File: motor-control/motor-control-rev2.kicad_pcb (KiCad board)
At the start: 2 copper layers, 122.3 x 65.9 mm, 80 parts, among them P1 CONN_02X12, P2 to_motor_phase_1, P3 to_motor_phase_2, P4 to_motor_phase_3, P5 CONN_01X01, P6 CONN_01X01, P7 CONN_01X04, Q1 csd19505kcs, Q10 csd19505kcs, Q11 csd19505kcs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

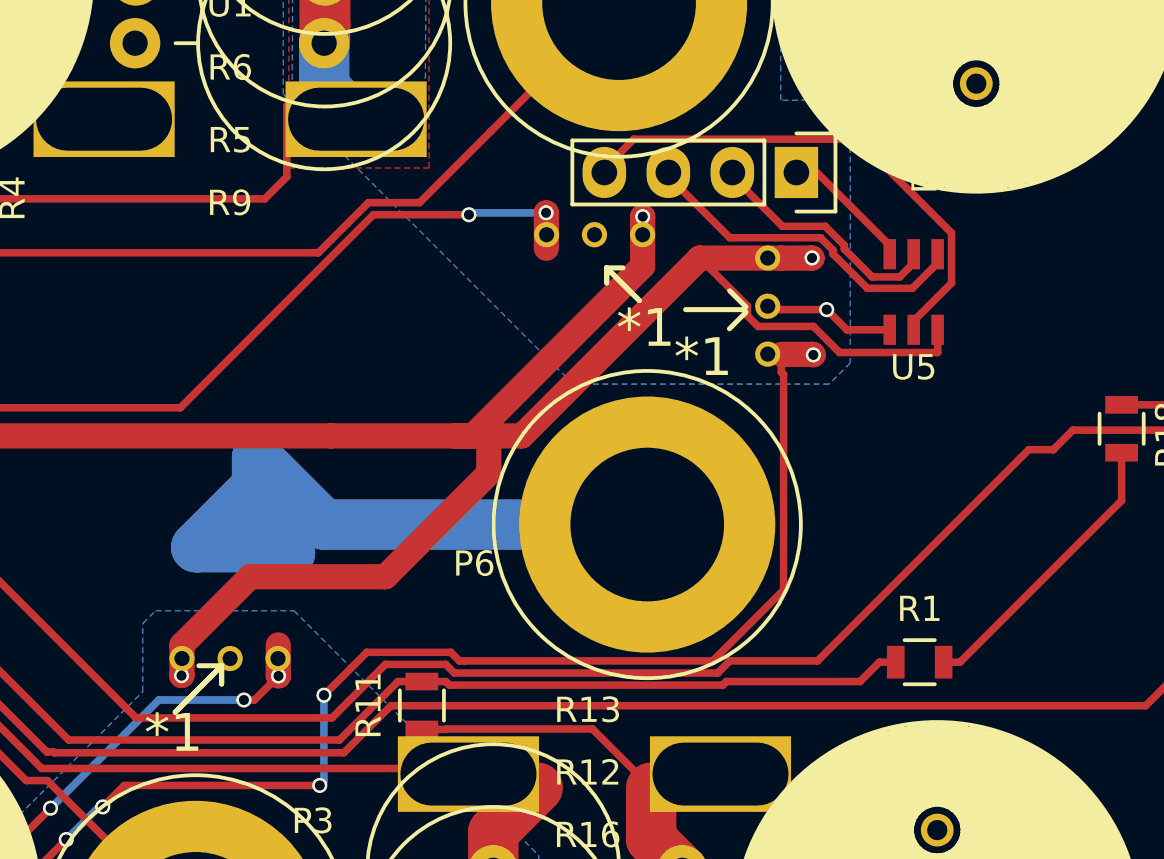
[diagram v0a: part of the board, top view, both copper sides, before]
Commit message: Added hall filtering components to pcb
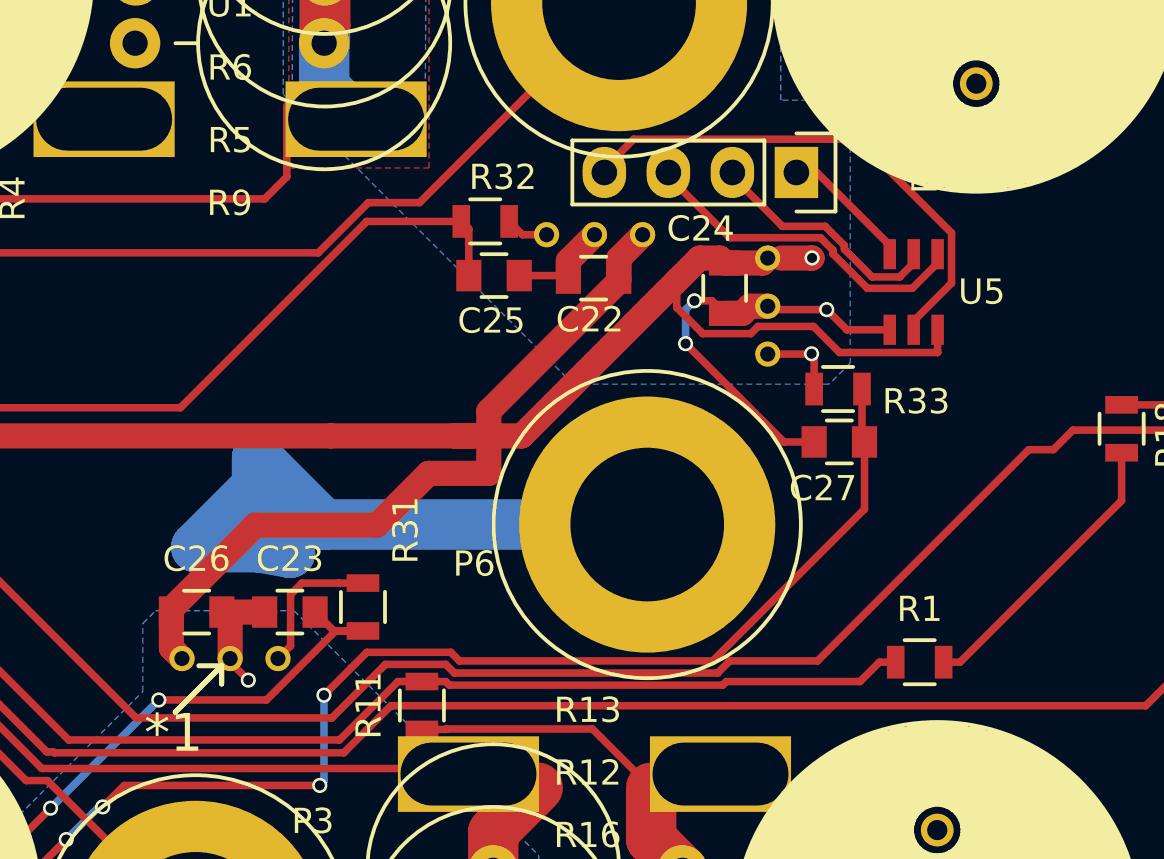
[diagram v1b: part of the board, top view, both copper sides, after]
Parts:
- added C22: 0.1uF, Capacitors_SMD:C_0805, F.Cu at (165.8, 80.2)
- added C23: 0.047uF, Capacitors_SMD:C_0805, F.Cu at (153.8, 93.4)
- added C24: 0.1uF, Capacitors_SMD:C_0805, F.Cu at (171.1, 80.5)
- added C25: 0.047uF, Capacitors_SMD:C_0805, F.Cu at (161.9, 80.0)
- added C26: 0.1uF, Capacitors_SMD:C_0805, F.Cu at (150.1, 93.4)
- added C27: 0.047uF, Capacitors_SMD:C_0805, F.Cu at (175.6, 86.7)
- added R31: 100R, Resistors_SMD:R_0805, F.Cu at (156.7, 93.2)
- added R32: 100R, Resistors_SMD:R_0805, F.Cu at (161.6, 77.9)
- added R33: 100R, Resistors_SMD:R_0805, F.Cu at (175.6, 84.5)
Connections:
- U1 pad 3: /power mosfets & current sensing/hall_1 -> Net-(R31-Pad1)
- U2 pad 3: /power mosfets & current sensing/hall_2 -> Net-(R32-Pad1)
- U3 pad 3: /power mosfets & current sensing/hall_3 -> Net-(R33-Pad2)
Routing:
- net GND: track 98.5 -> 119.2 mm, vias 9 -> 12
- net Net-(R31-Pad1): track 0.00 -> 5.81 mm
- net /power mosfets & current sensing/hall_1: track 51.4 -> 56.4 mm, vias 5 -> 4
- net Net-(R33-Pad2): track 0.00 -> 3.19 mm, vias 0 -> 1
- net /power mosfets & current sensing/hall_2: track 72.6 -> 70.0 mm, vias 4 -> 2
- net Net-(R32-Pad1): track 0.00 -> 1.70 mm
- net /power mosfets & current sensing/hall_3: track 76.6 -> 75.3 mm, vias 5 -> 4
- net VCC: track 183.9 -> 184.5 mm, vias 7 -> 5

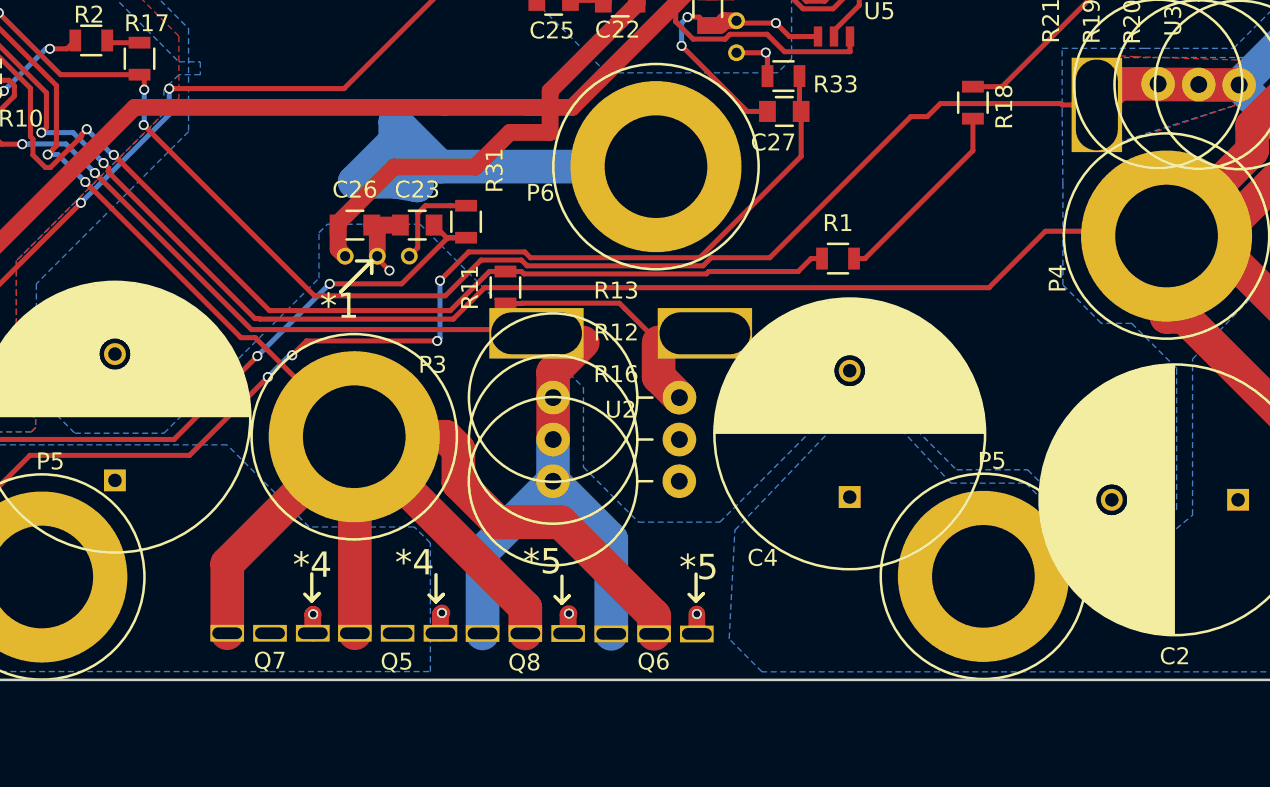
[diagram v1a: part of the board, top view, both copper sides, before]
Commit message: Began rework bottom fets spacing
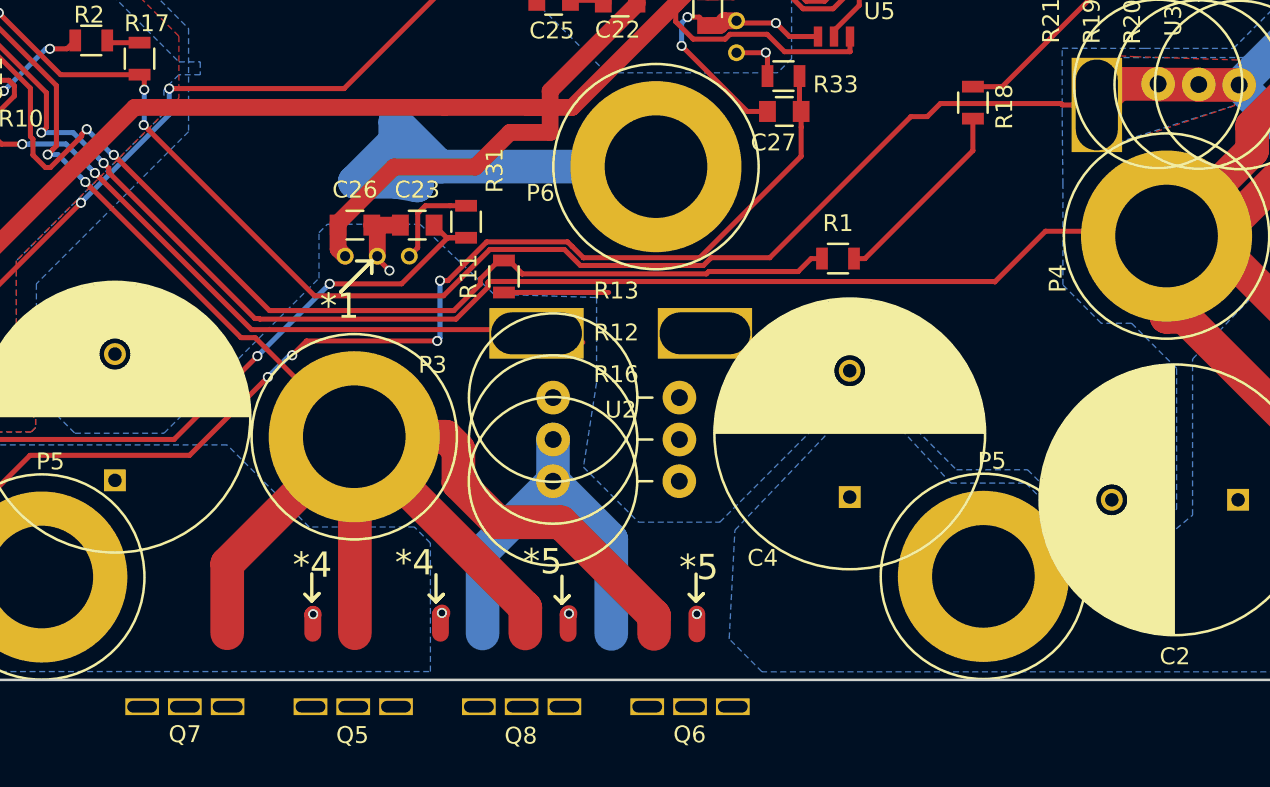
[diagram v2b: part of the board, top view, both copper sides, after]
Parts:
- moved Q7 6.68 mm to (140.0, 122.0)
- moved Q5 5.10 mm to (150.0, 122.0)
- moved Q6 4.82 mm to (170.0, 122.0)
- moved Q8 4.35 mm to (160.0, 122.0)
- moved R11 0.66 mm to (158.9, 96.5)
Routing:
- net GND: track 119.2 -> 111.6 mm
- net /Gate-Driver/SL_B: track 90.0 -> 83.5 mm
- net /Gate-Driver/SP2: track 68.8 -> 69.5 mm
- net /Gate-Driver/SL_C: track 119.3 -> 119.8 mm

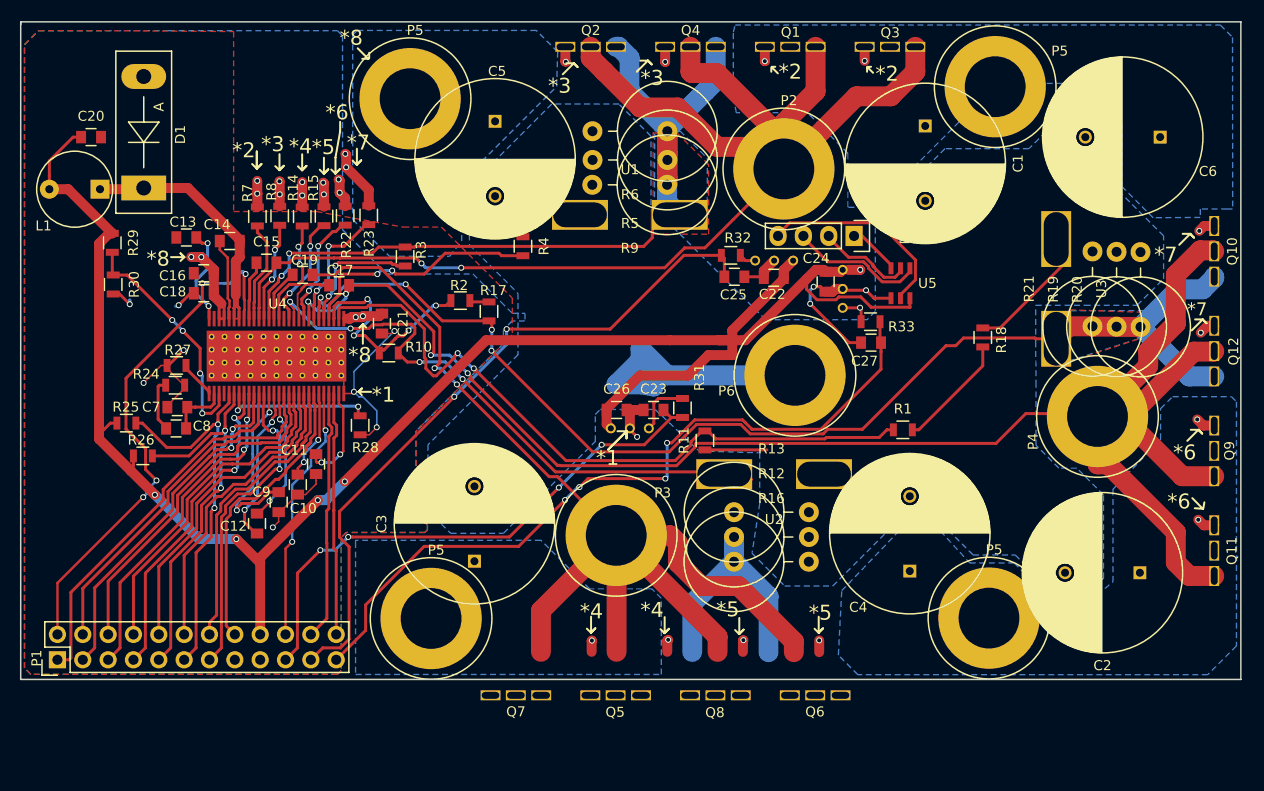
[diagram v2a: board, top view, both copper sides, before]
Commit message: Cont. work on bottom fets, fixed a no conn. on drv
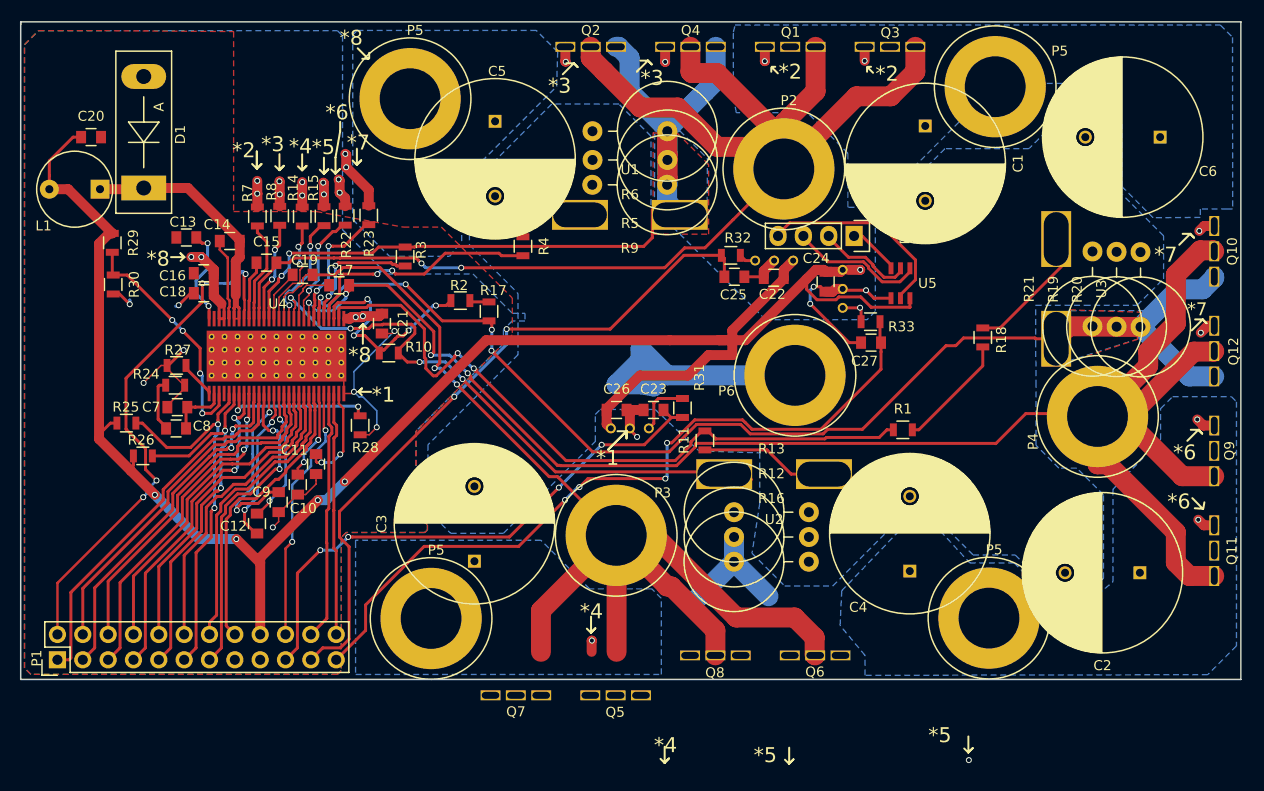
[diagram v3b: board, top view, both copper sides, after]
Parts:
- moved Q6 4.00 mm to (170.0, 118.0)
- moved Q8 4.00 mm to (160.0, 118.0)
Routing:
- net /Gate-Driver/SL_B: track 83.5 -> 73.6 mm
- net /Gate-Driver/SH_B: track 111.8 -> 120.4 mm
- net GND: track 111.6 -> 118.3 mm
- net Net-(Q5-Pad1): track 4.89 -> 2.50 mm, vias 4 -> 2
- net Net-(Q6-Pad1): track 4.83 -> 2.44 mm, vias 4 -> 2
- net (no net): track 0.00 -> 2.36 mm, vias 0 -> 3
- net VCC: track 184.5 -> 183.2 mm, vias 5 -> 4

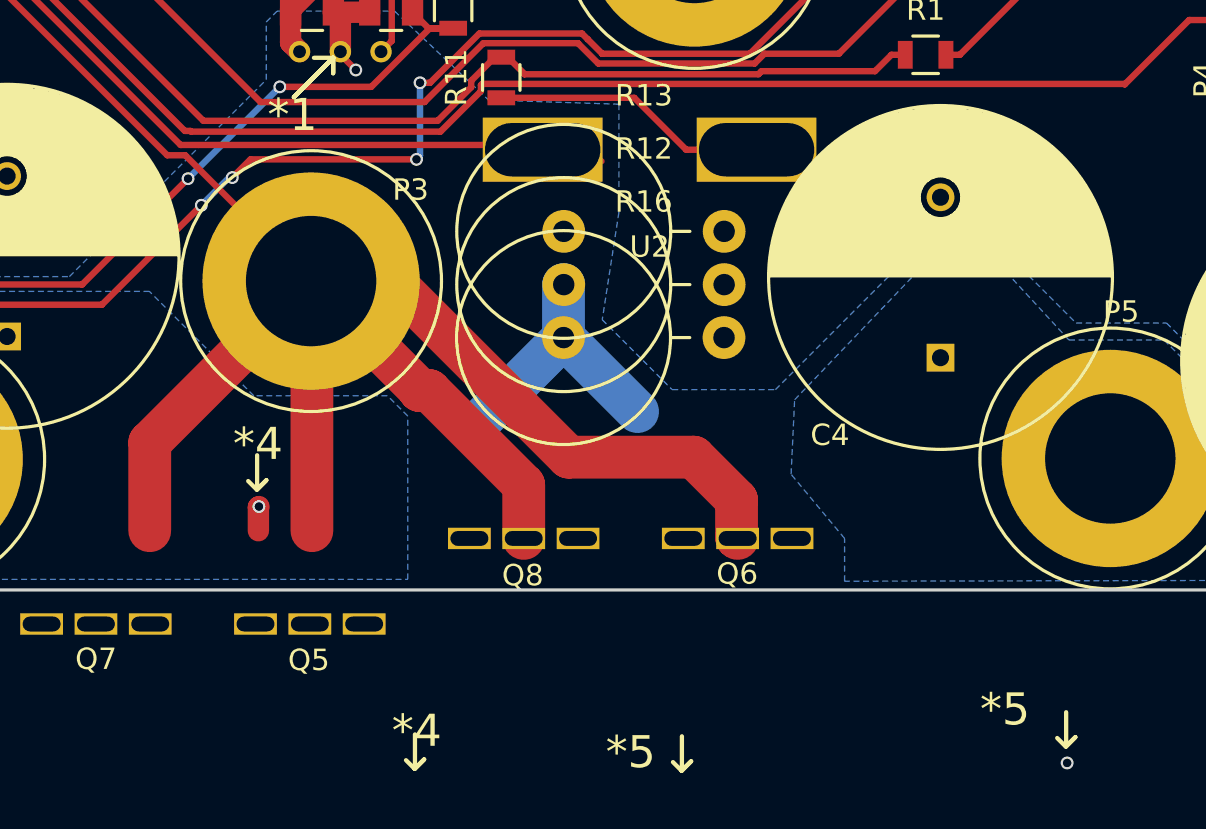
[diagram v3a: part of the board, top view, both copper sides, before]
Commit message: Continued work on bottom fets. Fixed a zone on top
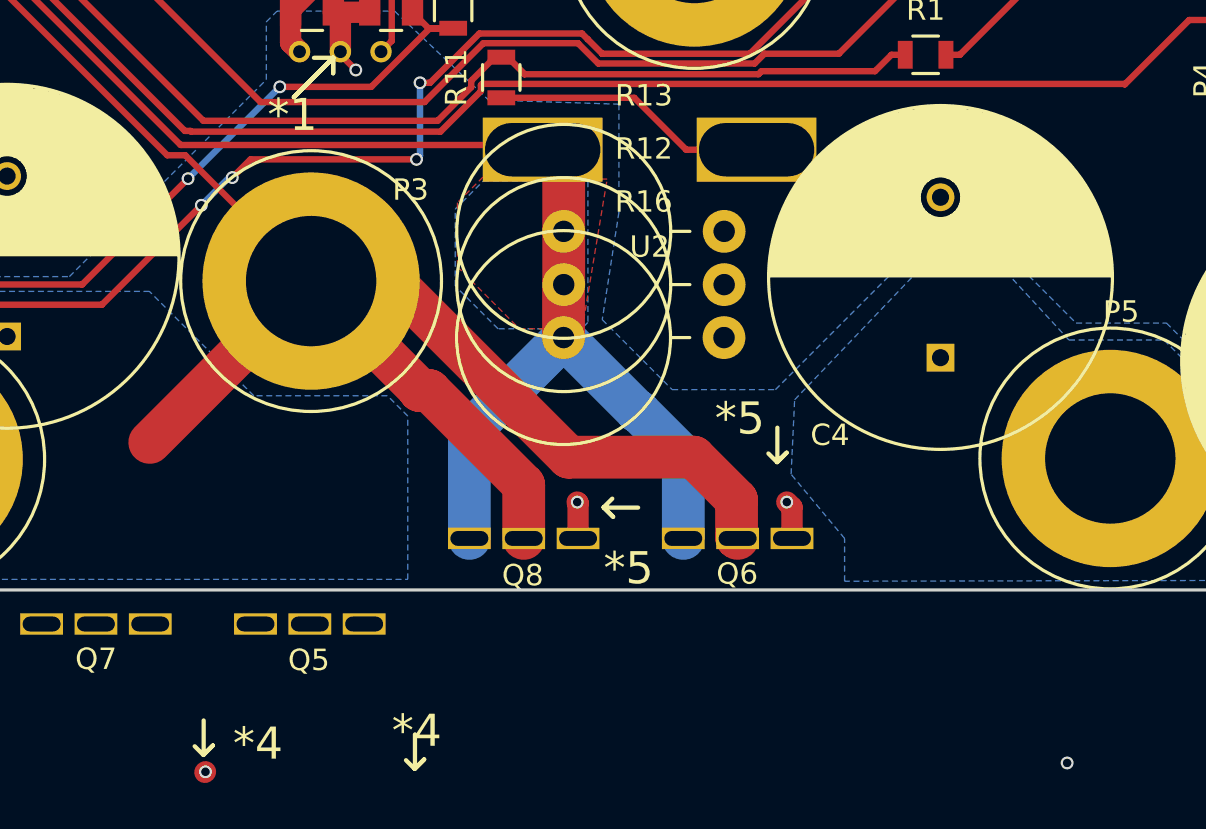
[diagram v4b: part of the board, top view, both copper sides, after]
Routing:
- net /Gate-Driver/SL_B: track 73.6 -> 89.6 mm
- net /Gate-Driver/SH_B: track 120.4 -> 104.6 mm
- net Net-(Q6-Pad1): track 2.44 -> 5.96 mm, vias 2 -> 4
- net (no net): track 2.36 -> 1.26 mm
- added copper zone on B.Cu, net /Gate-Driver/SL_B
- added copper zone on F.Cu, net /Gate-Driver/SL_B
